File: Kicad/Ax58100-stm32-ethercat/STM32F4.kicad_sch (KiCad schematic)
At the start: 34 parts, among them J1 Conn_01x06_Pin, J10 Conn_01x02_Pin, J11 Stepper 2, J12 Serial usart1, J13 Stepper 1, J3 Conn_01x06_Pin, J5 Conn_01x06_Pin, J9 STLINK, U5 AMS1117-3.3, Y2 8 MHz

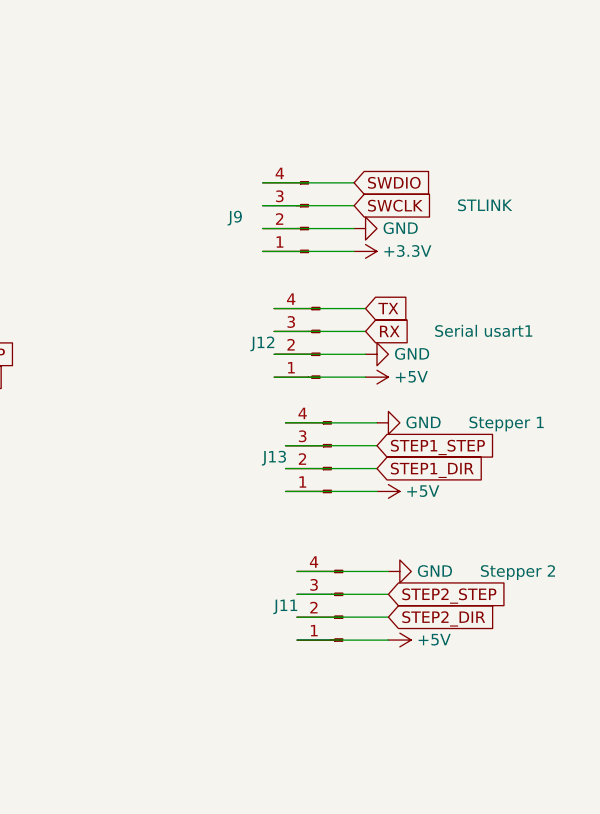
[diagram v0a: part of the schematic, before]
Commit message: Added optional pull-down to step generators
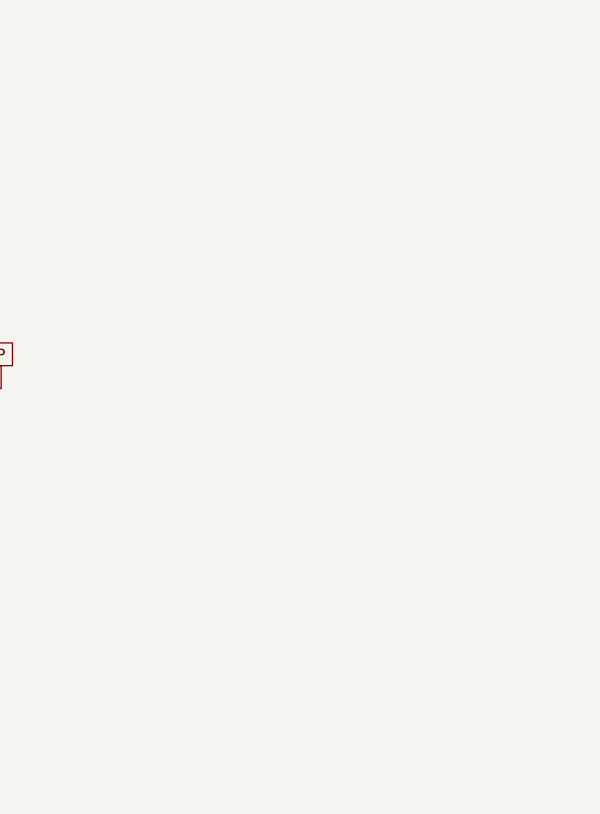
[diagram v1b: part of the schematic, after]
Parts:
- removed J11: Stepper 2, Connector_JST:JST_XH_B4B-XH-A_1x04_P2.50mm_Vertical, symbol Connector:Conn_01x04_Pin
- removed J12: Serial usart1, Connector_JST:JST_XH_B4B-XH-A_1x04_P2.50mm_Vertical, symbol Connector:Conn_01x04_Pin
- removed J13: Stepper 1, Connector_JST:JST_XH_B4B-XH-A_1x04_P2.50mm_Vertical, symbol Connector:Conn_01x04_Pin
- removed J9: STLINK, Connector_JST:JST_XH_B4B-XH-A_1x04_P2.50mm_Vertical, symbol Connector:Conn_01x04_Pin

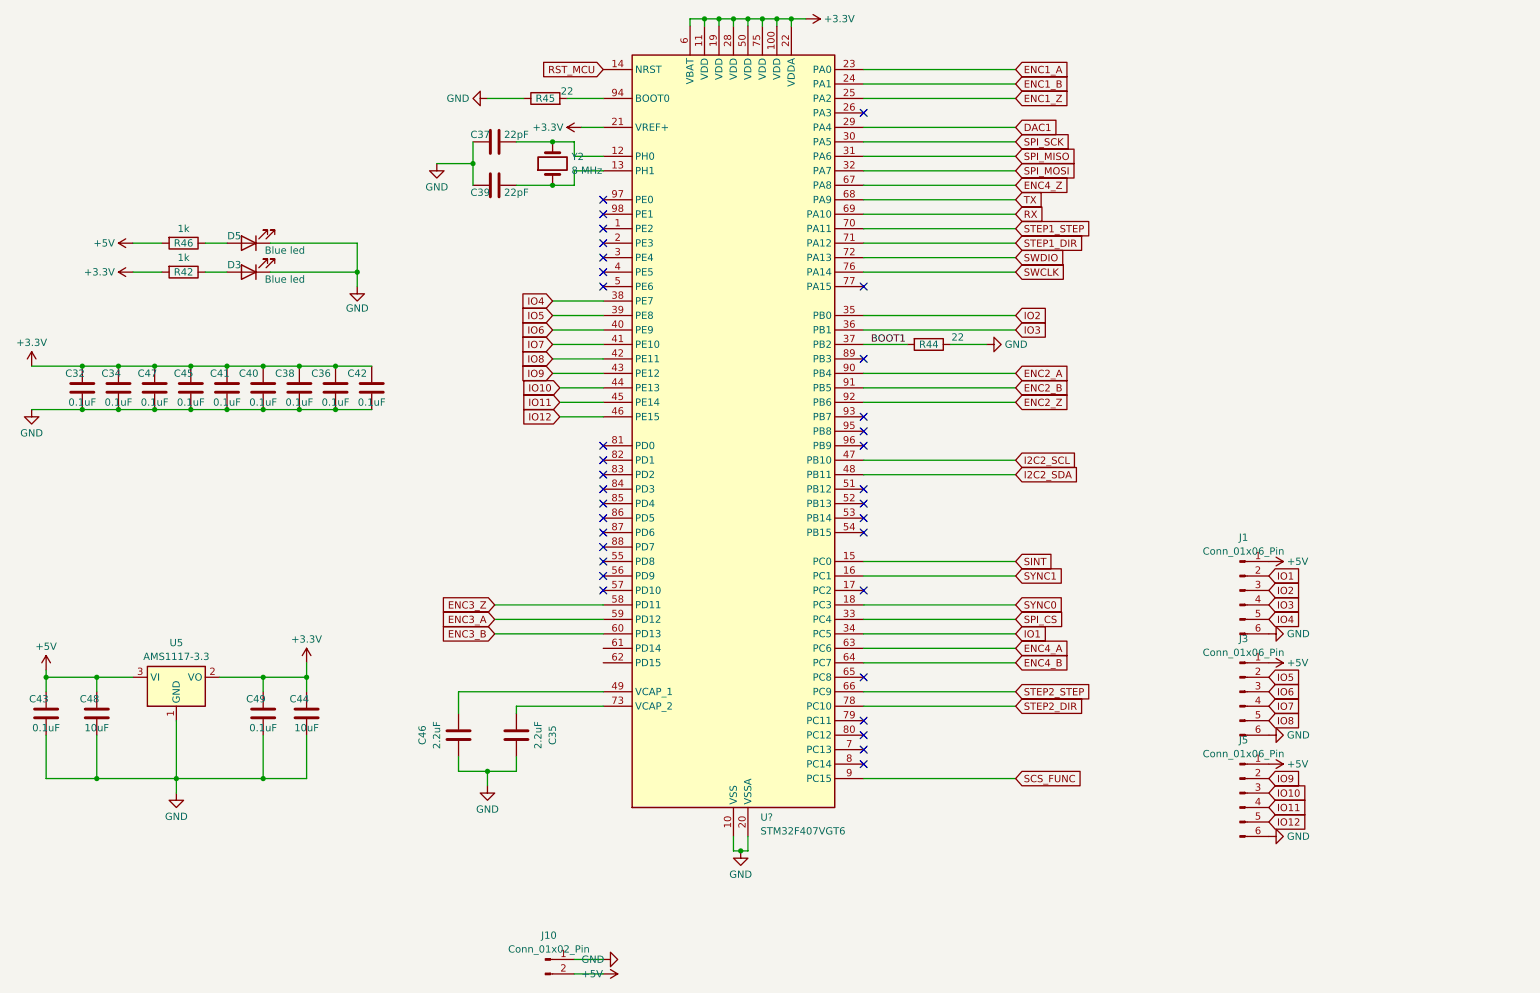
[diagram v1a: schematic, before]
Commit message: Steppers, encoders, IO, etc remapped
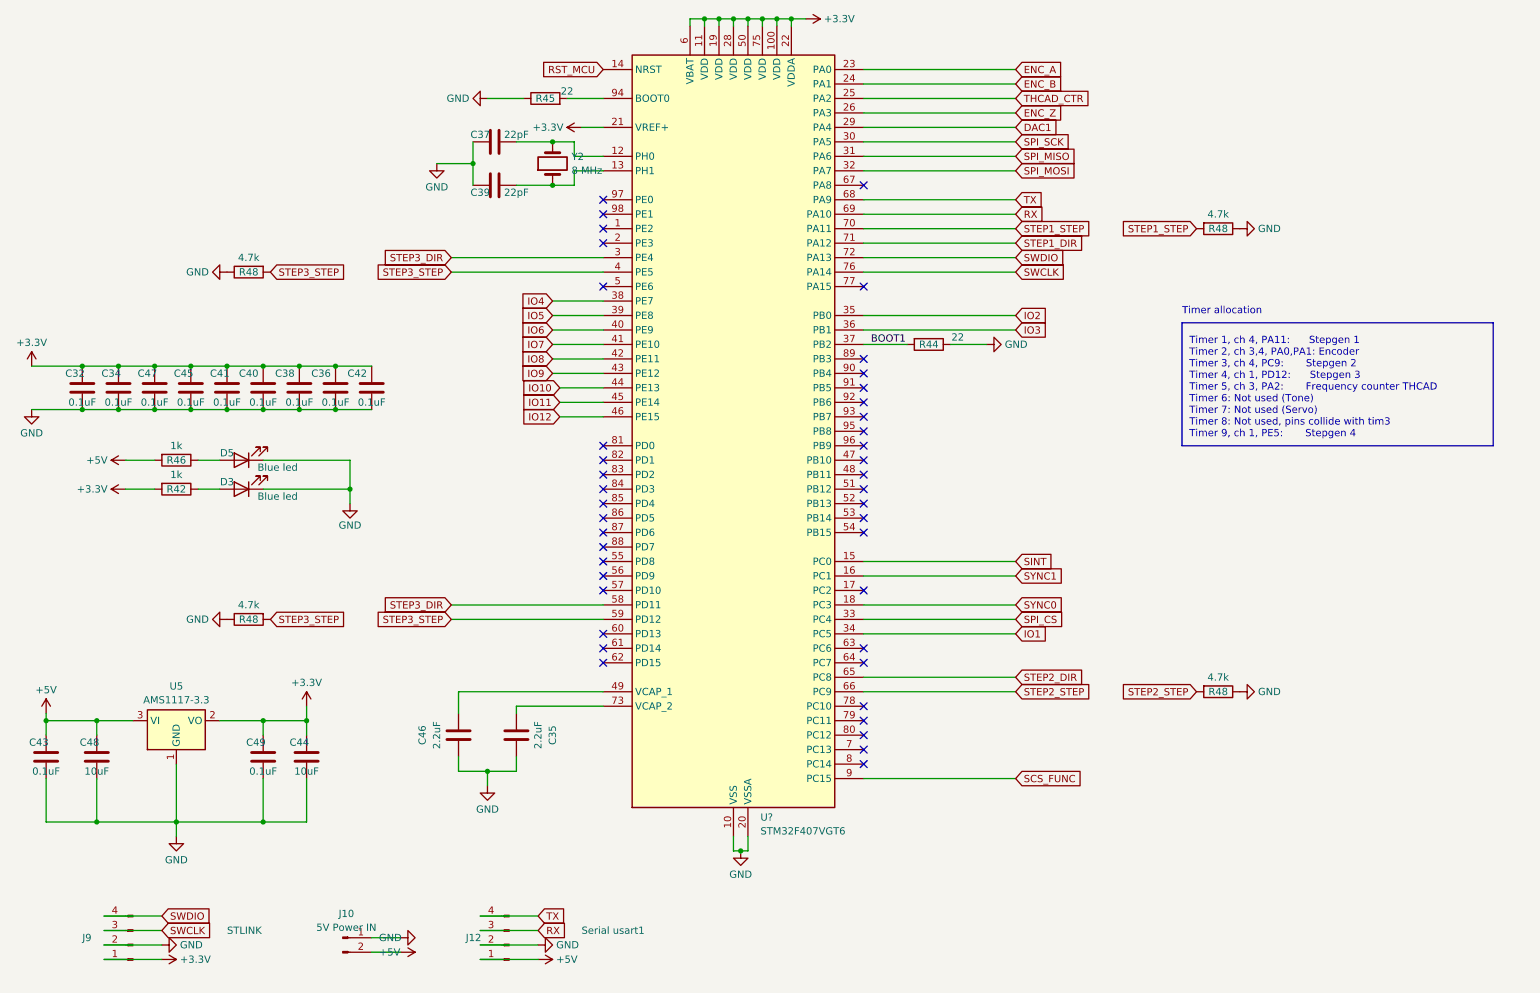
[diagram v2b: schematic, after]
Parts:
- removed J1, J3, J5: Conn_01x06_Pin, Connector_JST:JST_XH_B6B-XH-A_1x06_P2.50mm_Vertical, symbol Connector:Conn_01x06_Pin
- added J12: Serial usart1, Connector_JST:JST_XH_B4B-XH-A_1x04_P2.50mm_Vertical, symbol Connector:Conn_01x04_Pin
- added J9: STLINK, Connector_JST:JST_XH_B4B-XH-A_1x04_P2.50mm_Vertical, symbol Connector:Conn_01x04_Pin
- added R48 (x4): 4.7k, Resistor_SMD:R_0805_2012Metric, symbol Device:R
- J10: value Conn_01x02_Pin -> 5V Power IN
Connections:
- net ENC3_A is gone; now on net STEP3_STEP: U?.59 (PD12)
- net ENC3_Z is gone; now on net STEP3_DIR: U?.58 (PD11)
- net +3.3V: now also J9.1 (Pin_1)
- net +5V: now also J12.1 (Pin_1)
- net GND: now also J12.2 (Pin_2), J9.2 (Pin_2), R48.1, R48.1, R48.1, R48.1
- net RX: now also J12.3 (Pin_3)
- net STEP1_STEP: now also R48.2
- net STEP2_DIR: now also U?.65 (PC8); no longer U?.78 (PC10)
- net STEP2_STEP: now also R48.2
- net SWCLK: now also J9.3 (Pin_3)
- net SWDIO: now also J9.4 (Pin_4)
- net TX: now also J12.4 (Pin_4)
- net ENC_Z: now reaches U?.26 (PA3)
- net STEP3_DIR: now reaches U?.3 (PE4)
- net STEP3_STEP: now reaches U?.4 (PE5)
- net STEP3_STEP: now also R48.2, R48.2
- net ENC1_A renamed ENC_A
- net ENC1_B renamed ENC_B
- net ENC1_Z renamed THCAD_CTR
- net ENC2_A: no longer names the net of U?.90 (PB4)
- net ENC2_B: no longer names the net of U?.91 (PB5)
- net ENC2_Z: no longer names the net of U?.92 (PB6)
- net ENC3_B: no longer names the net of U?.60 (PD13)
- net ENC4_A: no longer names the net of U?.63 (PC6)
- net ENC4_B: no longer names the net of U?.64 (PC7)
- net ENC4_Z: no longer names the net of U?.67 (PA8)
- net I2C2_SCL: no longer names the net of U?.47 (PB10)
- net I2C2_SDA: no longer names the net of U?.48 (PB11)
- no-connect marks 34 -> 42
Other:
- note added: "Timer 1, ch 4, PA11: Stepgen 1 Timer 2, ch 3,4, PA0,PA1: Encoder Timer 3, ch 4, PC9: Stepgen 2 Timer 4, ch 1, PD12: Stepgen 3 Timer 5, ch 3, PA2: Frequency counter THCAD Timer 6: Not used (Tone) Timer 7: Not used (Servo) Timer 8: Not used, pins collide with tim3 Timer 9, ch 1, PE5: Stepgen 4"
- note added: "Timer allocation"
- title: (none) -> MetalMusings EaserCAT 3000
- moved on the sheet: C43, C44, C48, C49, D3, D5, J10, R42, R46, U5

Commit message: Assigned footprints
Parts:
- J10: footprint Connector_JST:JST_XH_B2B-XH-A_1x02_P2.50mm_Vertical -> TerminalBlock:TerminalBlock_bornier-2_P5.08mm
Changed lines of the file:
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@@
       (effects (font (size 1.27 1.27)))
     )
-    (property "Footprint" "Connector_JST:JST_XH_B2B-XH-A_1x02_P2.50mm_Vertical" (at 77.47 179.07 0)
+    (property "Footprint" "TerminalBlock:TerminalBlock_bornier-2_P5.08mm" (at 77.47 179.07 0)
       (effects (font (size 1.27 1.27)) hide)
     )

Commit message: First component placement
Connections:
- net STEP3_DIR: no longer U?.3 (PE4)
- net STEP3_STEP: no longer R48.2, U?.4 (PE5)
- new net STEP4_DIR: U?.3 (PE4)
- new net STEP4_STEP: R48.2, U?.4 (PE5)
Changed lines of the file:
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@@
     )
   )
-  (global_label "STEP3_STEP" (shape input) (at 96.52 62.23 180) (fields_autoplaced)
+  (global_label "STEP4_STEP" (shape input) (at 96.52 62.23 180) (fields_autoplaced)
     (effects (font (size 1.27 1.27)) (justify right))
     (property "Intersheetrefs" "${INTERSHEET_REFS}" (at 82.1655 62.23 0)
@@
     )
   )
-  (global_label "STEP3_DIR" (shape input) (at 96.52 59.69 180) (fields_autoplaced)
+  (global_label "STEP4_DIR" (shape input) (at 96.52 59.69 180) (fields_autoplaced)
     (effects (font (size 1.27 1.27)) (justify right))
     (property "Intersheetrefs" "${INTERSHEET_REFS}" (at 83.6168 59.69 0)
@@
     )
   )
-  (global_label "STEP3_STEP" (shape input) (at 64.77 62.23 0) (fields_autoplaced)
+  (global_label "STEP4_STEP" (shape input) (at 64.77 62.23 0) (fields_autoplaced)
     (effects (font (size 1.27 1.27)) (justify left))
     (property "Intersheetrefs" "${INTERSHEET_REFS}" (at 79.1245 62.23 0)

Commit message: wip
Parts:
- renumbered C32 to C1, C42 to C10, C49 to C11, C48 to C12, C45 to C13, C46 to C14, C47 to C15, C44 to C16, C43 to C17, C34 to C2, C36 to C3, C35 to C4, C37 to C5, C38 to C6, C39 to C7, C40 to C8, C41 to C9, D5 to D17, D3 to D19, J9 to J15, J12 to J16, R46 to R18, R45 to R19, R44 to R21, R42 to R22, U5 to U8, Y2 to Y1

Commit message: Might be in final shape.
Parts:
- J11: renamed from J10; footprint TerminalBlock:TerminalBlock_bornier-2_P5.08mm -> Connector_Phoenix_MC:PhoenixContact_MCV_1,5_2-G-3.5_1x02_P3.50mm_Vertical
- R48: value 4.7k -> 4k7
- renumbered C7 to C10, C8 to C11, C9 to C12, C12 to C13, C10 to C14, C17 to C15, C13 to C17, C14 to C18, C15 to C19, C11 to C26, C16 to C38, C2 to C4, C4 to C5, C1 to C6, C3 to C7, C5 to C8, C6 to C9, D19 to D18, J16 to J15, J15 to J17, R19 to R29, R18 to R38, R22 to R39, R21 to R40, U8 to U7

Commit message: all leds are now 0603
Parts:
- D17, D18: footprint LED_SMD:LED_0805_2012Metric -> LED_SMD:LED_0603_1608Metric
- Y1: footprint Crystal:Crystal_HC49-U_Vertical -> Crystal:Crystal_HC49-4H_Vertical
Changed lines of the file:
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@@
       (effects (font (size 1.27 1.27)))
     )
-    (property "Footprint" "LED_SMD:LED_0805_2012Metric" (at 59.69 95.25 0)
+    (property "Footprint" "LED_SMD:LED_0603_1608Metric" (at 59.69 95.25 0)
       (effects (font (size 1.27 1.27)) hide)
     )
@@
       (effects (font (size 1.27 1.27)))
     )
-    (property "Footprint" "LED_SMD:LED_0805_2012Metric" (at 59.69 100.33 0)
+    (property "Footprint" "LED_SMD:LED_0603_1608Metric" (at 59.69 100.33 0)
       (effects (font (size 1.27 1.27)) hide)
     )
@@
       (effects (font (size 1.27 1.27)) (justify right))
     )
-    (property "Footprint" "Crystal:Crystal_HC49-U_Vertical" (at 114.3 43.18 0)
-      (effects (font (size 1.27 1.27)) hide)
-    )
+    (property "Footprint" "Crystal:Crystal_HC49-4H_Vertical" (at 114.3 43.18 0)
+      (effects (font (size 1.27 1.27)) hide)
+    )
